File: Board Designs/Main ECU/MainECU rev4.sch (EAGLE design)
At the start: 164 parts, among them Q1 MMBT3904LT3G, Q11 MMBT3904LT3G, Q2 MMBT3904LT3G, Q3 MMBT3904LT3G, Q4 MMBT3904LT3G, Q5 MMBT3904LT3G, Q6 MMBT3904LT3G, Q7 MMBT3904LT3G, Q8 MMBT3904LT3G, Q9 MMBT3904LT3G, X1 CONNECTOR-37, X2 CONNECTOR-4AUTOSPORT, X3 CONNECTOR-4NANO-FIT-VERTICAL-4, X4 CONNECTOR-4NANO-FIT-VERTICAL-4

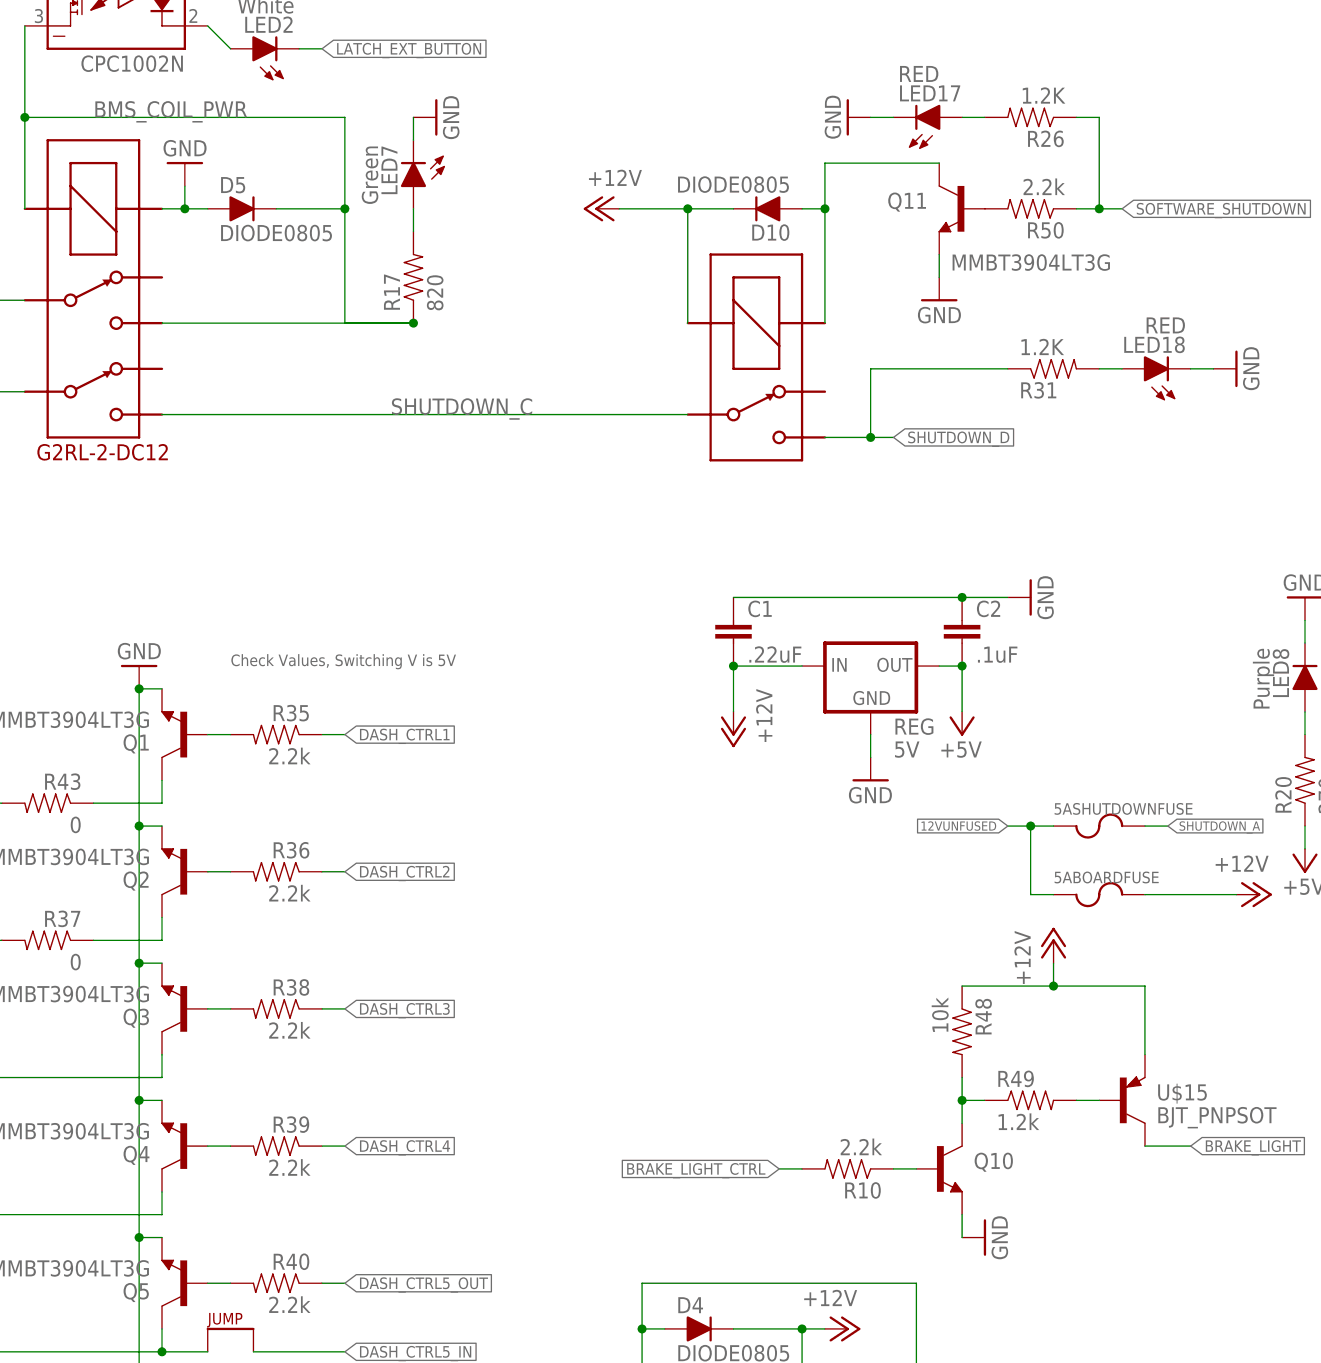
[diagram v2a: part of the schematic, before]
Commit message: Main ECU rev2/4: Add brake light NPN p/n
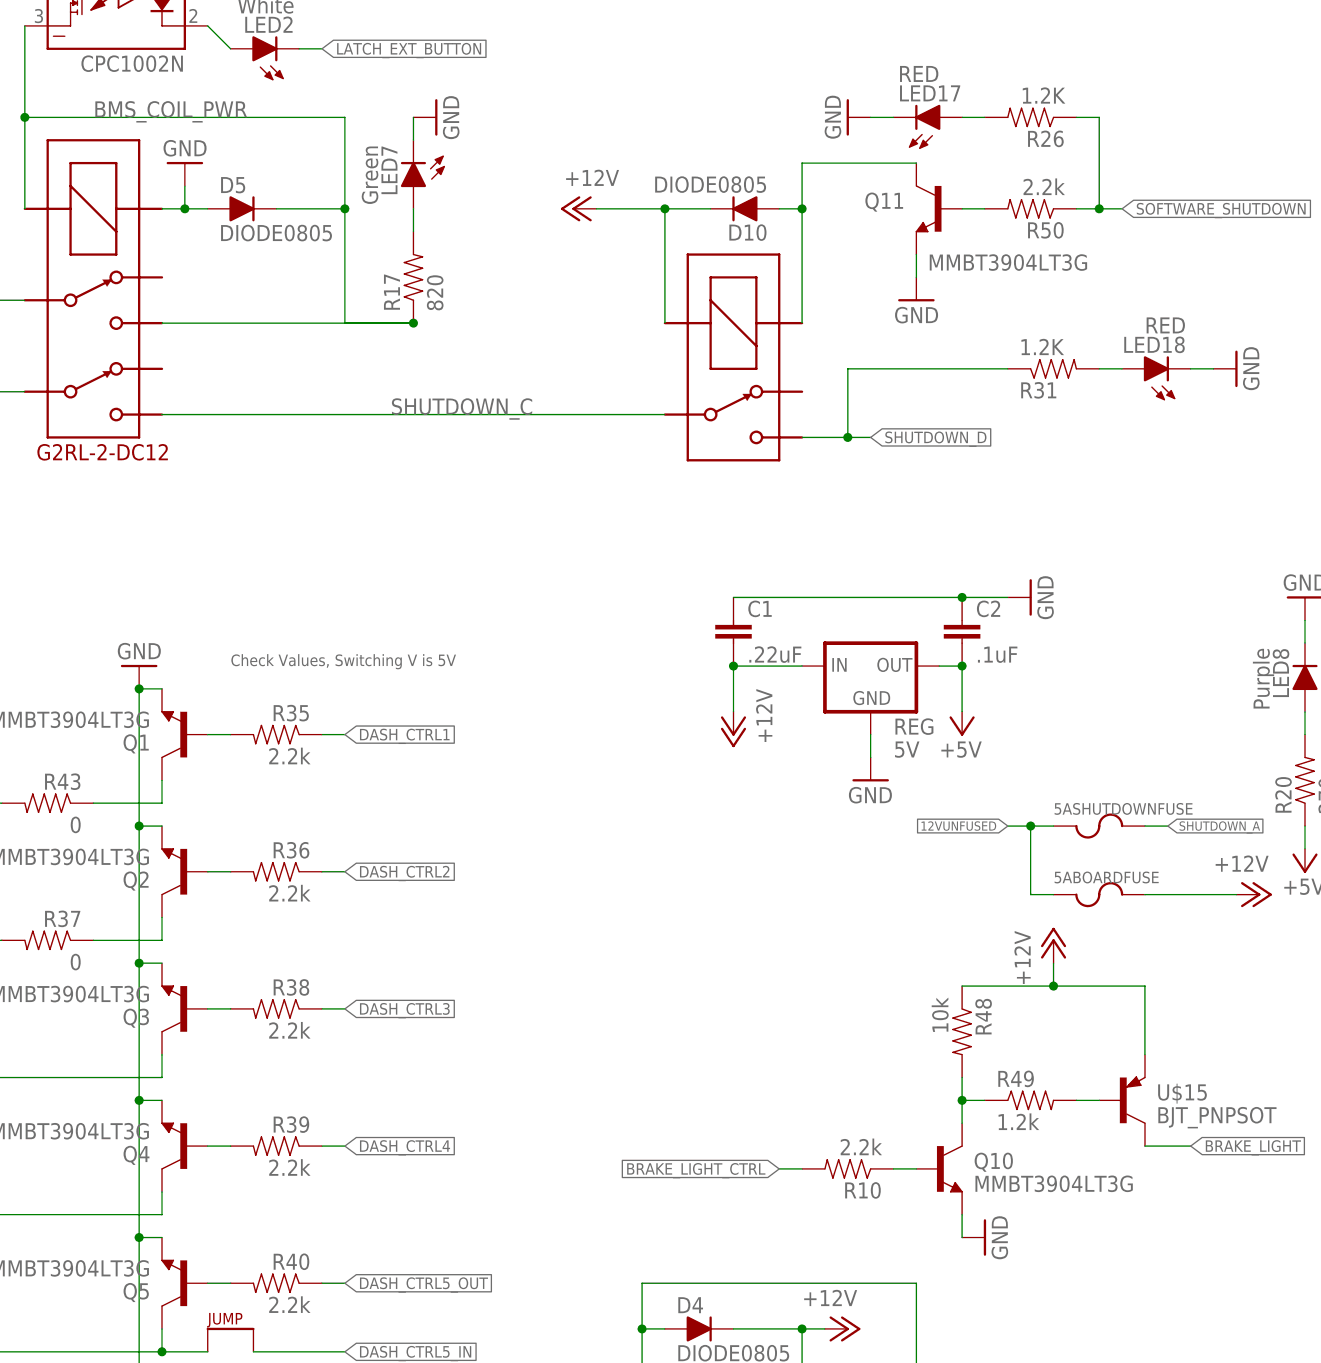
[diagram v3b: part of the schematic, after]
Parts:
- Q10: value (none) -> MMBT3904LT3G
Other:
- moved on the sheet: D10, Q11
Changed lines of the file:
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@@
 <part name="U$14" library="HyTechDevices" deviceset="JUMPER" device=""/>
 <part name="P+9" library="supply1" deviceset="+12V" device=""/>
-<part name="Q10" library="HyTechDevices" deviceset="BJT_NPN" device="SOT"/>
+<part name="Q10" library="HyTechDevices" deviceset="BJT_NPN" device="SOT" value="MMBT3904LT3G"/>
 <part name="U$15" library="HyTechDevices" deviceset="BJT_PNP" device="SOT"/>
 <part name="R10" library="HyTechDevices" deviceset="RESISTOR" device="0805-RES" value="2.2k"/>
@@
 <attribute name="VALUE" x="127" y="256.54" size="1.778" layer="96" rot="R90"/>
 </instance>
-<instance part="SOFTWARE_SHUTOFF" gate="G$1" x="182.88" y="193.04" smashed="yes" rot="R270"/>
-<instance part="P+23" gate="1" x="167.64" y="200.66" smashed="yes" rot="MR270">
-<attribute name="VALUE" x="172.72" y="203.2" size="1.778" layer="96" rot="MR0"/>
-</instance>
-<instance part="D10" gate="1" x="185.42" y="200.66" smashed="yes" rot="R180">
-<attribute name="NAME" x="189.23" y="198.9074" size="1.778" layer="95" rot="R180"/>
-<attribute name="VALUE" x="189.23" y="204.2414" size="1.778" layer="96" rot="R180"/>
+<instance part="SOFTWARE_SHUTOFF" gate="G$1" x="180.34" y="193.04" smashed="yes" rot="R270"/>
+<instance part="P+23" gate="1" x="165.1" y="200.66" smashed="yes" rot="MR270">
+<attribute name="VALUE" x="170.18" y="203.2" size="1.778" layer="96" rot="MR0"/>
+</instance>
+<instance part="D10" gate="1" x="182.88" y="200.66" smashed="yes" rot="R180">
+<attribute name="NAME" x="186.69" y="198.9074" size="1.778" layer="95" rot="R180"/>
+<attribute name="VALUE" x="186.69" y="204.2414" size="1.778" layer="96" rot="R180"/>
 </instance>
 <instance part="LED17" gate="LED" x="205.74" y="210.82" smashed="yes" rot="MR90">
@@
 <attribute name="VALUE" x="205.74" y="53.34" size="1.778" layer="96" rot="MR0"/>
 </instance>
-<instance part="Q11" gate="G$1" x="208.28" y="200.66" smashed="yes" rot="MR0">
-<attribute name="NAME" x="204.47" y="200.66" size="1.778" layer="95" rot="MR0"/>
-<attribute name="VALUE" x="207.01" y="195.58" size="1.778" layer="96" rot="MR180"/>
+<instance part="Q11" gate="G$1" x="205.74" y="200.66" smashed="yes" rot="MR0">
+<attribute name="NAME" x="201.93" y="200.66" size="1.778" layer="95" rot="MR0"/>
+<attribute name="VALUE" x="204.47" y="195.58" size="1.778" layer="96" rot="MR180"/>
 </instance>
-<instance part="GND11" gate="1" x="205.74" y="190.5" smashed="yes" rot="MR0">
-<attribute name="VALUE" x="208.28" y="187.96" size="1.778" layer="96" rot="MR0"/>
+<instance part="GND11" gate="1" x="203.2" y="190.5" smashed="yes" rot="MR0">
+<attribute name="VALUE" x="205.74" y="187.96" size="1.778" layer="96" rot="MR0"/>
 </instance>
 <instance part="R50" gate="G$1" x="215.9" y="200.66" smashed="yes" rot="R180">
@@
 <pinref part="Q11" gate="G$1" pin="EMITTER"/>
 <pinref part="GND11" gate="1" pin="GND"/>
-<wire x1="205.74" y1="195.58" x2="205.74" y2="193.04" width="0.1524" layer="91"/>
+<wire x1="203.2" y1="195.58" x2="203.2" y2="193.04" width="0.1524" layer="91"/>
 </segment>
 <segment>
@@
 <segment>
 <pinref part="D10" gate="1" pin="C"/>
-<wire x1="182.88" y1="200.66" x2="177.8" y2="200.66" width="0.1524" layer="91"/>
+<wire x1="180.34" y1="200.66" x2="175.26" y2="200.66" width="0.1524" layer="91"/>
 <pinref part="SOFTWARE_SHUTOFF" gate="G$1" pin="COIL-"/>
-<wire x1="177.8" y1="200.66" x2="177.8" y2="187.96" width="0.1524" layer="91"/>
+<wire x1="175.26" y1="200.66" x2="175.26" y2="187.96" width="0.1524" layer="91"/>
 <pinref part="P+23" gate="1" pin="+12V"/>
-<wire x1="170.18" y1="200.66" x2="177.8" y2="200.66" width="0.1524" layer="91"/>
-<junction x="177.8" y="200.66"/>
+<wire x1="167.64" y1="200.66" x2="175.26" y2="200.66" width="0.1524" layer="91"/>
+<junction x="175.26" y="200.66"/>
 </segment>
 <segment>
@@
 <segment>
 <pinref part="IMD_SHUTDOWN1" gate="G$1" pin="5"/>
-<wire x1="119.38" y1="177.8" x2="177.8" y2="177.8" width="0.1524" layer="91"/>
+<wire x1="119.38" y1="177.8" x2="175.26" y2="177.8" width="0.1524" layer="91"/>
 <pinref part="SOFTWARE_SHUTOFF" gate="G$1" pin="P"/>
 <label x="144.78" y="177.8" size="1.778" layer="95"/>
@@
 <segment>
 <pinref part="SOFTWARE_SHUTOFF" gate="G$1" pin="S"/>
-<wire x1="193.04" y1="175.26" x2="198.12" y2="175.26" width="0.1524" layer="91"/>
+<wire x1="190.5" y1="175.26" x2="195.58" y2="175.26" width="0.1524" layer="91"/>
 <pinref part="R31" gate="G$1" pin="1"/>
-<wire x1="198.12" y1="175.26" x2="200.66" y2="175.26" width="0.1524" layer="91"/>
-<wire x1="213.36" y1="182.88" x2="198.12" y2="182.88" width="0.1524" layer="91"/>
-<wire x1="198.12" y1="182.88" x2="198.12" y2="175.26" width="0.1524" layer="91"/>
-<junction x="198.12" y="175.26"/>
-<label x="200.66" y="175.26" size="1.27" layer="95" xref="yes"/>
+<wire x1="195.58" y1="175.26" x2="198.12" y2="175.26" width="0.1524" layer="91"/>
+<wire x1="213.36" y1="182.88" x2="195.58" y2="182.88" width="0.1524" layer="91"/>
+<wire x1="195.58" y1="182.88" x2="195.58" y2="175.26" width="0.1524" layer="91"/>
+<junction x="195.58" y="175.26"/>
+<label x="198.12" y="175.26" size="1.27" layer="95" xref="yes"/>
 </segment>
 <segment>
@@
 <pinref part="Q11" gate="G$1" pin="BASE"/>
 <pinref part="R50" gate="G$1" pin="2"/>
+<wire x1="208.28" y1="200.66" x2="210.82" y2="200.66" width="0.1524" layer="91"/>
 </segment>
 </net>
@@
 <pinref part="SOFTWARE_SHUTOFF" gate="G$1" pin="COIL+"/>
 <pinref part="D10" gate="1" pin="A"/>
-<wire x1="190.5" y1="200.66" x2="193.04" y2="200.66" width="0.1524" layer="91"/>
-<wire x1="193.04" y1="200.66" x2="193.04" y2="187.96" width="0.1524" layer="91"/>
+<wire x1="187.96" y1="200.66" x2="190.5" y2="200.66" width="0.1524" layer="91"/>
+<wire x1="190.5" y1="200.66" x2="190.5" y2="187.96" width="0.1524" layer="91"/>
 <pinref part="Q11" gate="G$1" pin="COLLECTOR"/>
-<wire x1="205.74" y1="205.74" x2="193.04" y2="205.74" width="0.1524" layer="91"/>
-<wire x1="193.04" y1="205.74" x2="193.04" y2="200.66" width="0.1524" layer="91"/>
-<junction x="193.04" y="200.66"/>
+<wire x1="203.2" y1="205.74" x2="190.5" y2="205.74" width="0.1524" layer="91"/>
+<wire x1="190.5" y1="205.74" x2="190.5" y2="200.66" width="0.1524" layer="91"/>
+<junction x="190.5" y="200.66"/>
 </segment>
 </net>

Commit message: Main ECU rev3/4: Update silkscreen for manufacturing, Main ECU rev4: switch to high-side dashboard switching and flip parts on wrong side
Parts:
- removed Q1, Q2, Q3, Q4, Q5, Q6, Q7, Q8: MMBT3904LT3G, HyTechDevices:BJT_NPNSOT
- added LED12, LED13, LED4: Red, HyTechDevices:LED-0805
- added R25, R51, R52: 100, HyTechDevices:RESISTOR0805-RES
- added U$29, U$30: TLP291-4, HyTechDevices:TLP291-4
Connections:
- new net N$69: LED4.C, R25.1
- new net N$70: LED12.C, R51.1
- new net N$71: LED13.C, R52.1
- net +12V: now also U$29.C1, U$29.C2, U$29.C3, U$29.C4, U$30.C1, U$30.C2, U$30.C3, U$30.C4
- net DASH_IO3: now also U$29.EM3; no longer Q3.COLLECTOR
- net DASH_IO4: now also U$29.EM4; no longer Q4.COLLECTOR
- net DASH_IO5: now also U$30.EM1; no longer Q5.COLLECTOR
- net DASH_IO6: now also U$30.EM2; no longer Q6.COLLECTOR
- net DASH_IO7: now also U$30.EM3; no longer Q7.COLLECTOR
- net DASH_IO8: now also U$30.EM4; no longer Q8.COLLECTOR
- net FAN1CONTROL: now also LED4.A
- net FAN2CONTROL: now also LED13.A
- net GND: now also R25.2, R51.2, R52.2, U$29.GND1, U$29.GND2, U$29.GND3, U$29.GND4, U$30.GND1, U$30.GND2, U$30.GND3, U$30.GND4; no longer Q1.EMITTER, Q2.EMITTER, Q3.EMITTER, Q4.EMITTER, Q5.EMITTER, Q6.EMITTER, Q7.EMITTER, Q8.EMITTER
- net N$30: now also U$29.VCC2; no longer Q2.BASE
- net N$42: now also U$29.EM2; no longer Q2.COLLECTOR
- net N$51: now also U$29.VCC1; no longer Q1.BASE
- net N$52: now also U$29.VCC3; no longer Q3.BASE
- net N$53: now also U$29.VCC4; no longer Q4.BASE
- net N$54: now also U$30.VCC1; no longer Q5.BASE
- net N$55: now also U$30.VCC2; no longer Q6.BASE
- net N$56: now also U$30.VCC3; no longer Q7.BASE
- net N$57: now also U$30.VCC4; no longer Q8.BASE
- net N$59: now also U$29.EM1; no longer Q1.COLLECTOR
- net PUMPCONTROL: now also LED12.A
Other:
- moved on the sheet: BOARD_TEMP, R35, R36, R37, R38, R39, R40, R41, R42, R43, R44, R9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
